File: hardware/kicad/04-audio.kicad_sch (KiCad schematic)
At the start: 9 parts, among them U5 PAM8403

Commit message: fix(audio): bias PAM8403 INL/INR to VREF, not GND (R4-HIGH-3)
The two generators disagreed, in their own comments, about the same parts:

  routing.py:2912  "R20 (20k): INL (pin 7) bias to GND"
  audio.py:137     "biases INL node to VREF (pin 8), NOT to GND ... Tying to
                    GND fights the internal bias and produces asymmetric
                    clipping." (PAM8403 datasheet Fig. 3)

Fix R4-HIGH-3 was applied to the schematic and never propagated to the
routing, so the fabricated board ties both bias resistors to GND -- exactly
the failure its own comment warns about. It surfaced as 4 of the pin-to-net
mismatches in verify_netlist_diff.

Copper change: R20.1 and R21.1 move from GND to PAM_VREF via a new bias rail.
The three far pads (C21.1, R20.1, R21.1) all sit at x=38.95, so the rail runs
down that lane -- SPK+ B.Cu is at x=40.00 (gap 0.80mm), +5V B.Cu at x=38.00
(gap 0.60mm), and nothing crosses the span. Going UP from R20.1 is blocked by
C21.1 (GND), so the rail reaches VREF through a jog at y=25.20, threading
between the C21 GND via (top edge 24.80, gap 0.30mm) and the +5V via (bottom
edge 25.55, gap 0.25mm). Two GND stubs and their vias are removed: 321 -> 319
vias, 604 -> 606 segments.

audio.py places R20/R21 with angle=180 so schematic pin 1 is the VREF end,
matching pad 1 on the board. Without it the NETS agree while the pin NUMBERS
stay swapped and the gate still fails.

verify_polarity expected R20.1/R21.1 == GND -- it encoded the routing bug, so
it passed while the two sides disagreed. Updated to PAM_VREF with the reason.

Verified: DFM 122/0, DFA 9/0, polarity 48/48, native DRC 0 violations,
power-net integrity 5/5 single group, zone-fill sanity PASS, gerber integrity
33/0, JLCPCB validation 24/0, connectivity PASS. verify_netlist_diff 17 -> 13
mismatches. verify-all 52/54 -- the 2 failures are pre-existing on main
(VBUS 0.273mm width x4, and the remaining netlist pin-numbering mismatches),
neither touched by this change.

release_jlcpc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
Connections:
- net PAM_IN_AC: now also R20.2, R21.2; no longer R20.1, R21.1
- net PAM_VREF: now also R20.1, R21.1; no longer R20.2, R21.2
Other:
- moved on the sheet: R20, R21
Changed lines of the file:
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@@
   (global_label "PAM_IN_AC" (shape output) (at 82 100 0) (effects (font (size 1.27 1.27))) (property "Intersheetrefs" "" (at 0 0 0) (effects (font (size 1.27 1.27)) hide)))
   (text "DC-block (in series, I2S_DOUT -> PAM_IN_AC)" (at 56 93 0) (effects (font (size 1.5 1.5)) (justify left)))
-  (symbol (lib_id "R") (at 70 134 0) (unit 1) (exclude_from_sim no) (in_bom yes) (on_board yes) (dnp no) (property "Reference" "R20" (at 70 129 0) (effects (font (size 1.27 1.27)))) (property "Value" "20k" (at 70 139 0) (effects (font (size 1.27 1.27)))) (pin "1") (pin "2") (instances (project "esp32-emu-turbo" (path "/00000005-cafe-4000-8000-000000000005" (reference "R20") (unit 1)))))
+  (symbol (lib_id "R") (at 70 134 180) (unit 1) (exclude_from_sim no) (in_bom yes) (on_board yes) (dnp no) (property "Reference" "R20" (at 70 129 0) (effects (font (size 1.27 1.27)))) (property "Value" "20k" (at 70 139 0) (effects (font (size 1.27 1.27)))) (pin "1") (pin "2") (instances (project "esp32-emu-turbo" (path "/00000005-cafe-4000-8000-000000000005" (reference "R20") (unit 1)))))
   (wire (pts (xy 70 130.19) (xy 70 128)) (stroke (width 0) (type default)))
   (global_label "PAM_IN_AC" (shape input) (at 70 128 90) (effects (font (size 1.27 1.27))) (property "Intersheetrefs" "" (at 0 0 0) (effects (font (size 1.27 1.27)) hide)))
@@
   (global_label "PAM_VREF" (shape input) (at 70 140 270) (effects (font (size 1.27 1.27))) (property "Intersheetrefs" "" (at 0 0 0) (effects (font (size 1.27 1.27)) hide)))
   (text "INL bias -> PAM_VREF" (at 62 148 0) (effects (font (size 1.5 1.5)) (justify left)))
-  (symbol (lib_id "R") (at 70 150 0) (unit 1) (exclude_from_sim no) (in_bom yes) (on_board yes) (dnp no) (property "Reference" "R21" (at 70 145 0) (effects (font (size 1.27 1.27)))) (property "Value" "20k" (at 70 155 0) (effects (font (size 1.27 1.27)))) (pin "1") (pin "2") (instances (project "esp32-emu-turbo" (path "/00000005-cafe-4000-8000-000000000005" (reference "R21") (unit 1)))))
+  (symbol (lib_id "R") (at 70 150 180) (unit 1) (exclude_from_sim no) (in_bom yes) (on_board yes) (dnp no) (property "Reference" "R21" (at 70 145 0) (effects (font (size 1.27 1.27)))) (property "Value" "20k" (at 70 155 0) (effects (font (size 1.27 1.27)))) (pin "1") (pin "2") (instances (project "esp32-emu-turbo" (path "/00000005-cafe-4000-8000-000000000005" (reference "R21") (unit 1)))))
   (wire (pts (xy 70 146.19) (xy 70 144)) (stroke (width 0) (type default)))
   (global_label "PAM_IN_AC" (shape input) (at 70 144 90) (effects (font (size 1.27 1.27))) (property "Intersheetrefs" "" (at 0 0 0) (effects (font (size 1.27 1.27)) hide)))

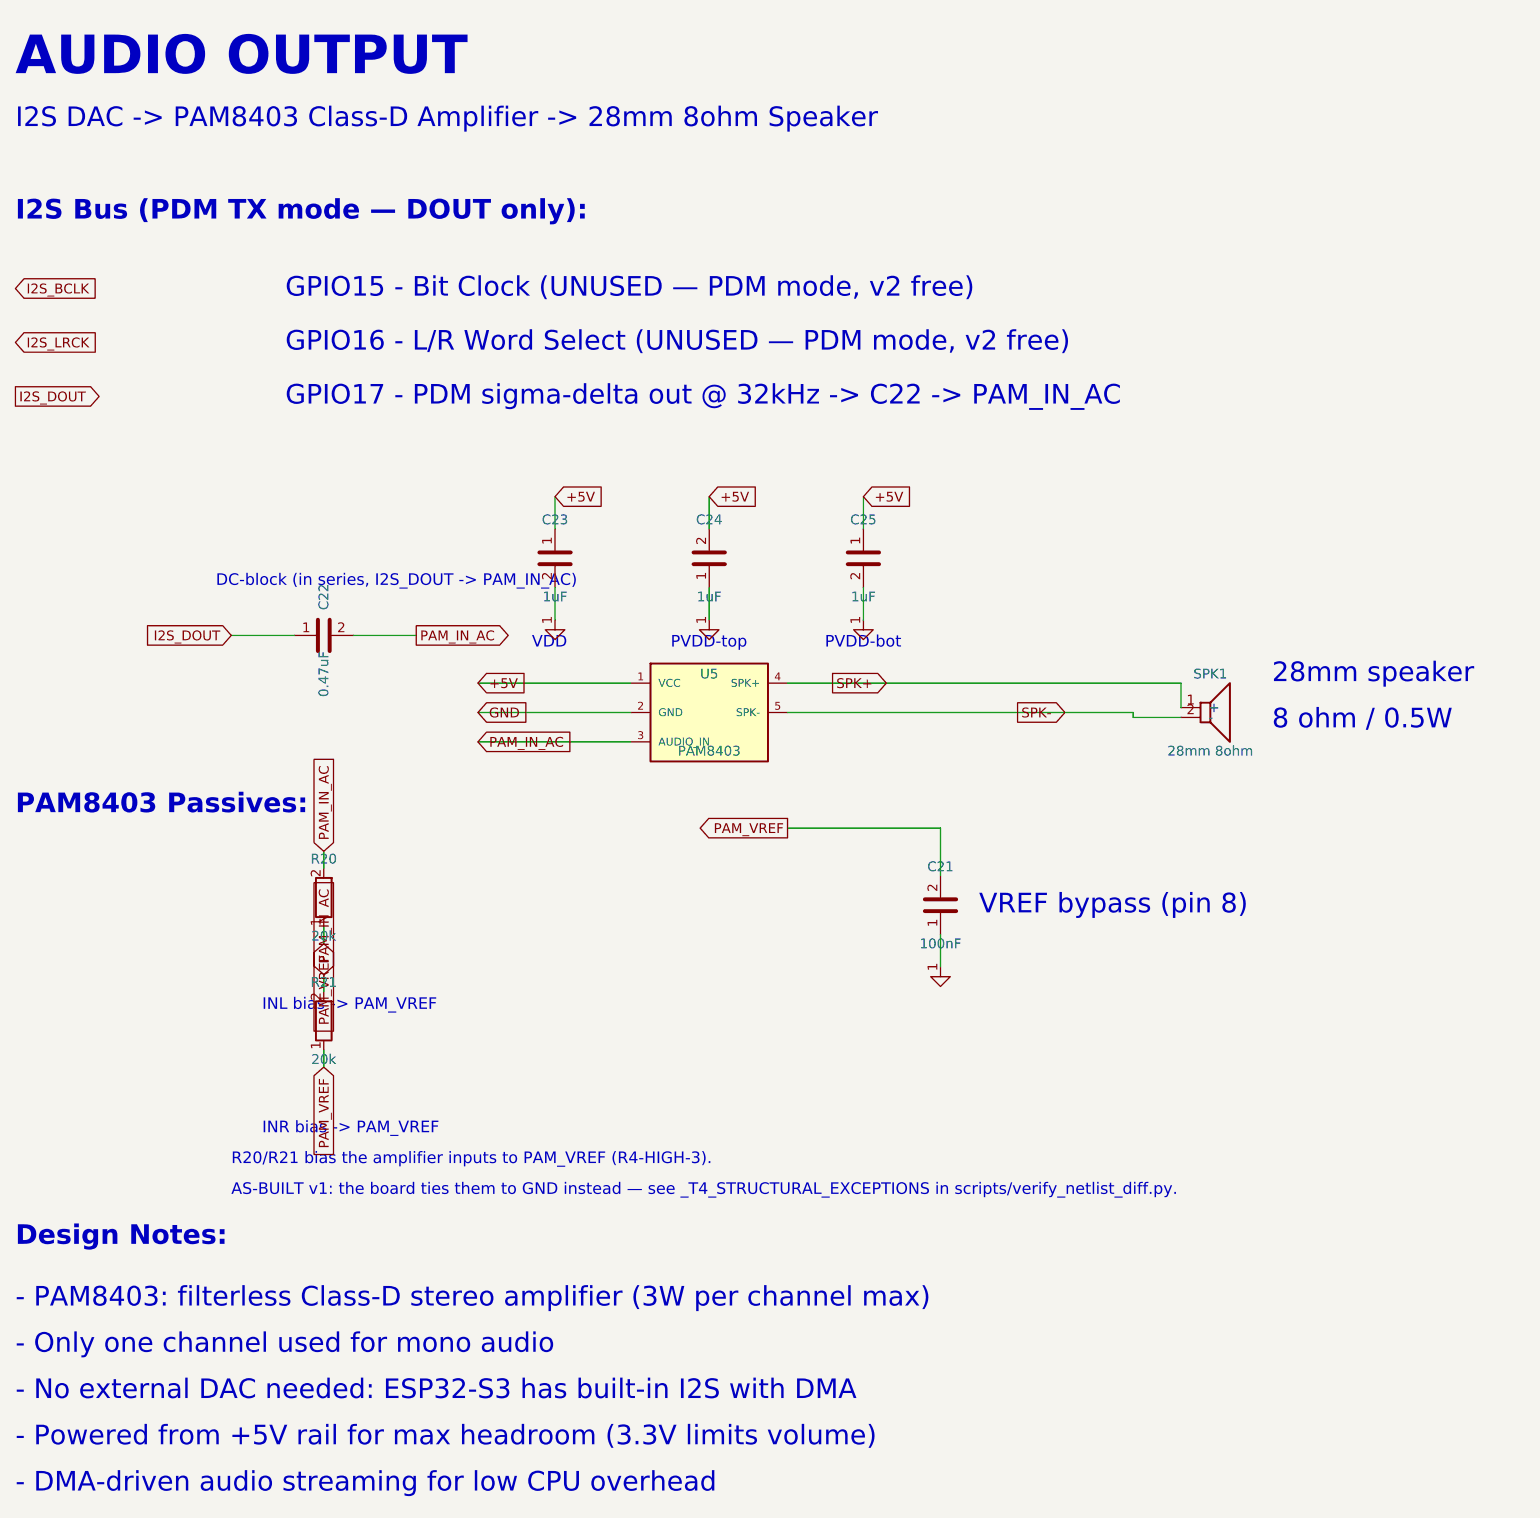
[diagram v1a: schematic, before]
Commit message: sch: nothing printable may overlap — new legibility gate, 14 overlaps cleared
Sister gate to verify_schematic_crossings.py. That one guarantees no WIRE
crosses another; this one guarantees no LABEL, JUNCTION or TEXT lands on top
of another item. Same reason: a schematic that is electrically correct but
unreadable cannot be reviewed, and an unreviewable schematic is where
net-level bugs hide -- as the (power) flag bug just demonstrated.

verify_schematic_overlaps.py boxes every printable item (text, label,
global_label, junction, and symbol Reference/Value fields) and reports any
pair with real overlapping area. Text width is measured at 0.72 * size per
character, conservatively under KiCad's true stroke-font advance, so a
reported overlap is ink on ink rather than a rounding artefact.

The box model handles all four orientations separately -- 0 extends +x, 180
-x, 90 -y, 270 +y. Getting that wrong matters: the first version treated 90
and 270 alike and invented 4 overlaps that were not on the page.

Overlaps fixed, 14 -> 0 across 488 items on 7 sheets. No sheet needed
splitting; there was room on all of them.

  01-power-supply  two note lines both emitted at ny+36 (227 mm² of text on
                   text -- the ladder skipped a step), plus "HF bypass",
                   "Charging", "USB ESD TVS" sitting on labels/refs, and the
                   R16 Reference field on the +5V rail junction.
  04-audio         R20/R21's vertical PAM_VREF / PAM_IN_AC labels grew ~7.3mm
                   along the stub axis toward each other and collided, and at
                   6mm the stub put each label on its own symbol's Value
                   field. Now horizontal labels on 8mm stubs, R21 moved 20mm
                   below R20 instead of 16mm.

R16 needed a value threading two constraints half a millimetre apart: at 76.0
its Reference hit the junction, at 79.0 its KEY stub reached y=86.6 and
crossed the IP5306 wire at y=85 -- caught by the crossings gate after the
firs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
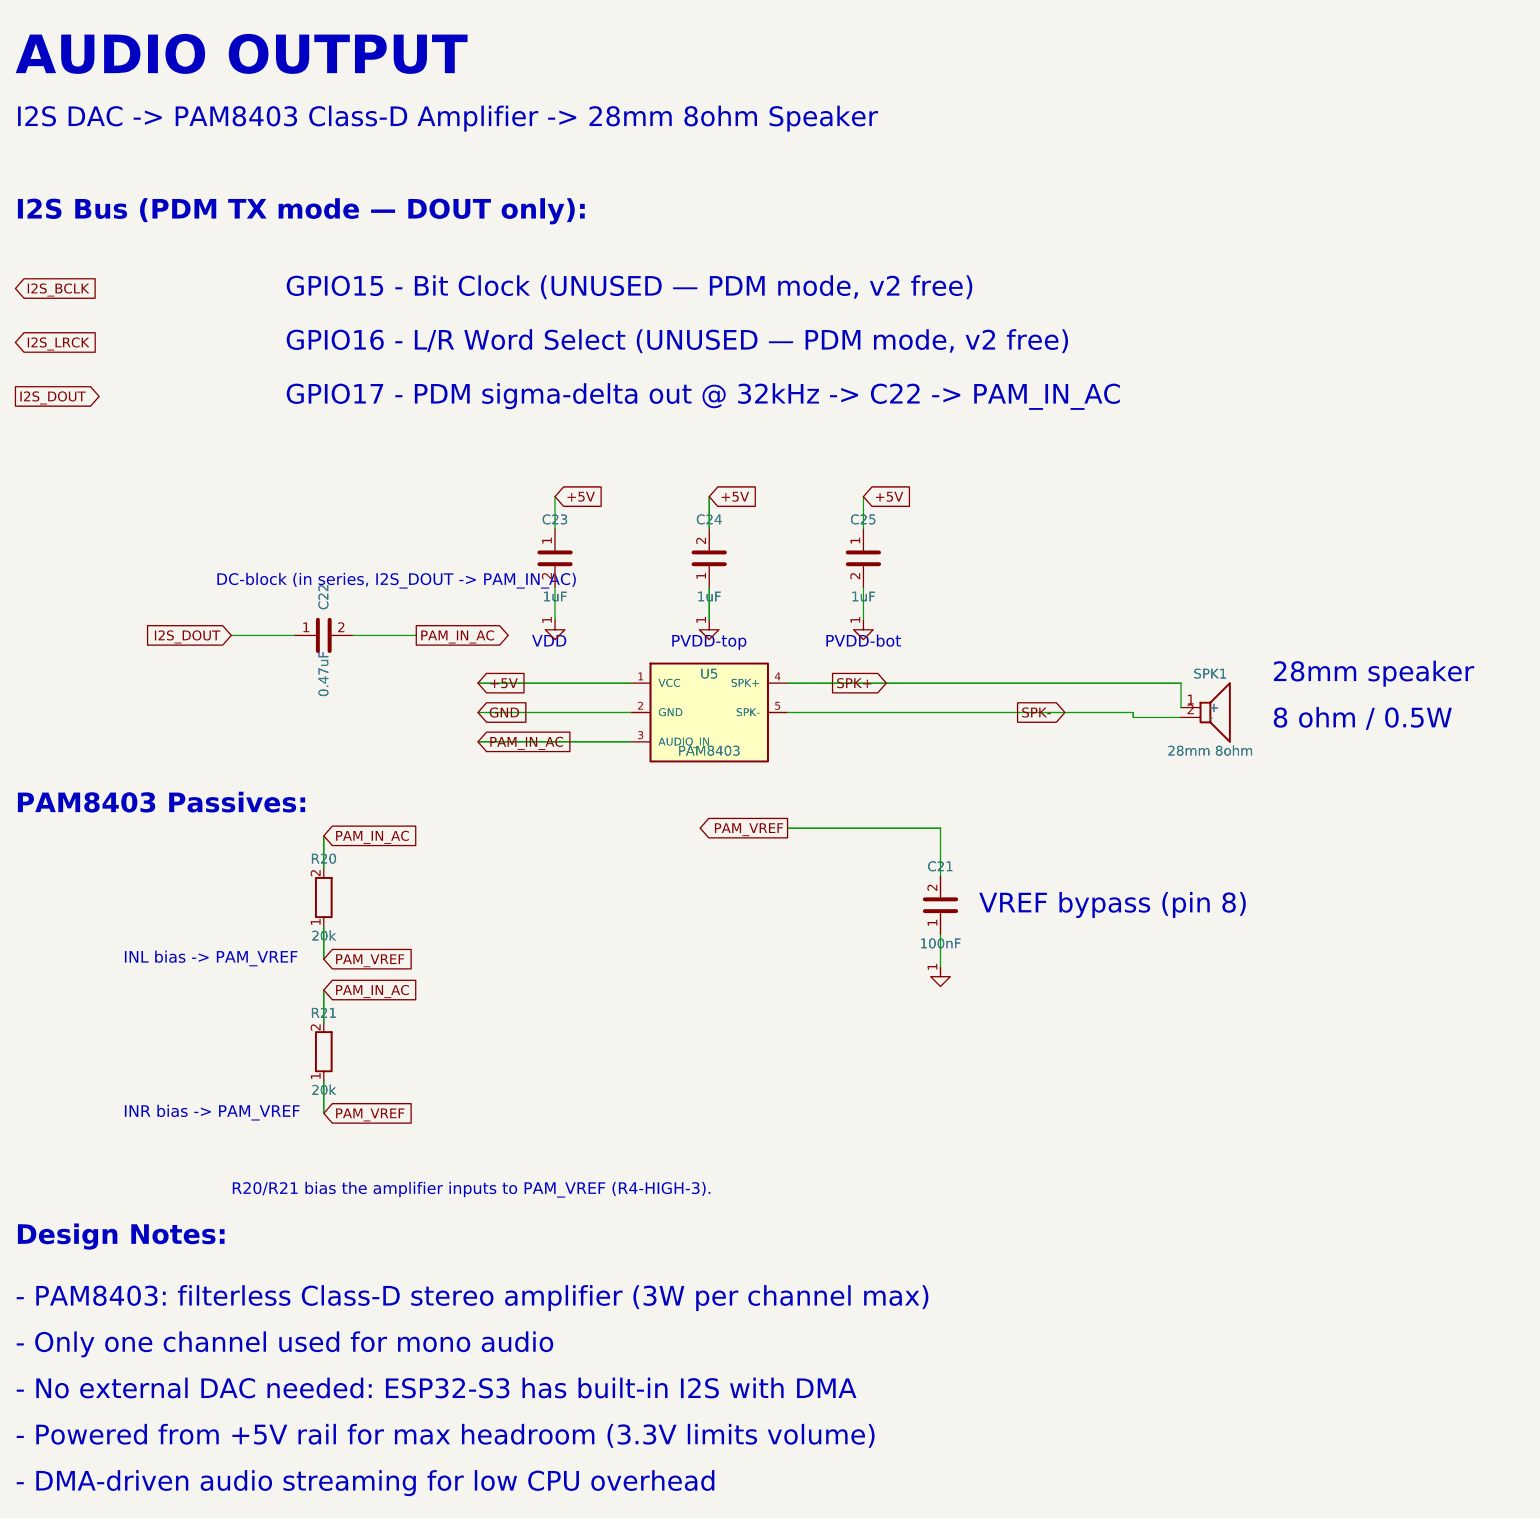
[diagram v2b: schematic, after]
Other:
- note removed: "AS-BUILT v1: the board ties them to GND instead — see _T4_STRUCTURAL_EXCEPTIONS in scripts/verify_netlist_diff.py."
- moved on the sheet: R21
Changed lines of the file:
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@@
   (text "DC-block (in series, I2S_DOUT -> PAM_IN_AC)" (at 56 93 0) (effects (font (size 1.5 1.5)) (justify left)))
   (symbol (lib_id "R") (at 70 134 180) (unit 1) (exclude_from_sim no) (in_bom yes) (on_board yes) (dnp no) (property "Reference" "R20" (at 70 129 0) (effects (font (size 1.27 1.27)))) (property "Value" "20k" (at 70 139 0) (effects (font (size 1.27 1.27)))) (pin "1") (pin "2") (instances (project "esp32-emu-turbo" (path "/00000005-cafe-4000-8000-000000000005" (reference "R20") (unit 1)))))
-  (wire (pts (xy 70 130.19) (xy 70 128)) (stroke (width 0) (type default)))
-  (global_label "PAM_IN_AC" (shape input) (at 70 128 90) (effects (font (size 1.27 1.27))) (property "Intersheetrefs" "" (at 0 0 0) (effects (font (size 1.27 1.27)) hide)))
-  (wire (pts (xy 70 137.81) (xy 70 140)) (stroke (width 0) (type default)))
-  (global_label "PAM_VREF" (shape input) (at 70 140 270) (effects (font (size 1.27 1.27))) (property "Intersheetrefs" "" (at 0 0 0) (effects (font (size 1.27 1.27)) hide)))
-  (text "INL bias -> PAM_VREF" (at 62 148 0) (effects (font (size 1.5 1.5)) (justify left)))
-  (symbol (lib_id "R") (at 70 150 180) (unit 1) (exclude_from_sim no) (in_bom yes) (on_board yes) (dnp no) (property "Reference" "R21" (at 70 145 0) (effects (font (size 1.27 1.27)))) (property "Value" "20k" (at 70 155 0) (effects (font (size 1.27 1.27)))) (pin "1") (pin "2") (instances (project "esp32-emu-turbo" (path "/00000005-cafe-4000-8000-000000000005" (reference "R21") (unit 1)))))
-  (wire (pts (xy 70 146.19) (xy 70 144)) (stroke (width 0) (type default)))
-  (global_label "PAM_IN_AC" (shape input) (at 70 144 90) (effects (font (size 1.27 1.27))) (property "Intersheetrefs" "" (at 0 0 0) (effects (font (size 1.27 1.27)) hide)))
-  (wire (pts (xy 70 153.81) (xy 70 156)) (stroke (width 0) (type default)))
-  (global_label "PAM_VREF" (shape input) (at 70 156 270) (effects (font (size 1.27 1.27))) (property "Intersheetrefs" "" (at 0 0 0) (effects (font (size 1.27 1.27)) hide)))
-  (text "INR bias -> PAM_VREF" (at 62 164 0) (effects (font (size 1.5 1.5)) (justify left)))
-  (text "R20/R21 bias the amplifier inputs to PAM_VREF (R4-HIGH-3)." (at 58 168 0) (effects (font (size 1.5 1.5)) (justify left)))
-  (text "AS-BUILT v1: the board ties them to GND instead — see _T4_STRUCTURAL_EXCEPTIONS in scripts/verify_netlist_diff.py." (at 58 172 0) (effects (font (size 1.5 1.5)) (justify left)))
+  (wire (pts (xy 70 130.19) (xy 70 126)) (stroke (width 0) (type default)))
+  (global_label "PAM_IN_AC" (shape input) (at 70 126 0) (effects (font (size 1.27 1.27))) (property "Intersheetrefs" "" (at 0 0 0) (effects (font (size 1.27 1.27)) hide)))
+  (wire (pts (xy 70 137.81) (xy 70 142)) (stroke (width 0) (type default)))
+  (global_label "PAM_VREF" (shape input) (at 70 142 0) (effects (font (size 1.27 1.27))) (property "Intersheetrefs" "" (at 0 0 0) (effects (font (size 1.27 1.27)) hide)))
+  (text "INL bias -> PAM_VREF" (at 44 142 0) (effects (font (size 1.5 1.5)) (justify left)))
+  (symbol (lib_id "R") (at 70 154 180) (unit 1) (exclude_from_sim no) (in_bom yes) (on_board yes) (dnp no) (property "Reference" "R21" (at 70 149 0) (effects (font (size 1.27 1.27)))) (property "Value" "20k" (at 70 159 0) (effects (font (size 1.27 1.27)))) (pin "1") (pin "2") (instances (project "esp32-emu-turbo" (path "/00000005-cafe-4000-8000-000000000005" (reference "R21") (unit 1)))))
+  (wire (pts (xy 70 150.19) (xy 70 146)) (stroke (width 0) (type default)))
+  (global_label "PAM_IN_AC" (shape input) (at 70 146 0) (effects (font (size 1.27 1.27))) (property "Intersheetrefs" "" (at 0 0 0) (effects (font (size 1.27 1.27)) hide)))
+  (wire (pts (xy 70 157.81) (xy 70 162)) (stroke (width 0) (type default)))
+  (global_label "PAM_VREF" (shape input) (at 70 162 0) (effects (font (size 1.27 1.27))) (property "Intersheetrefs" "" (at 0 0 0) (effects (font (size 1.27 1.27)) hide)))
+  (text "INR bias -> PAM_VREF" (at 44 162 0) (effects (font (size 1.5 1.5)) (justify left)))
+  (text "R20/R21 bias the amplifier inputs to PAM_VREF (R4-HIGH-3)." (at 58 172 0) (effects (font (size 1.5 1.5)) (justify left)))
   (symbol (lib_id "C") (at 100 90 0) (unit 1) (exclude_from_sim no) (in_bom yes) (on_board yes) (dnp no) (property "Reference" "C23" (at 100 85 0) (effects (font (size 1.27 1.27)))) (property "Value" "1uF" (at 100 95 0) (effects (font (size 1.27 1.27)))) (pin "1") (pin "2") (instances (project "esp32-emu-turbo" (path "/00000005-cafe-4000-8000-000000000005" (reference "C23") (unit 1)))))
   (global_label "+5V" (shape input) (at 100 82 0) (effects (font (size 1.27 1.27))) (property "Intersheetrefs" "" (at 0 0 0) (effects (font (size 1.27 1.27)) hide)))
